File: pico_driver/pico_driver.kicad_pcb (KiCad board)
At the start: 4 copper layers, 65 x 56 mm, 25 parts, among them J1 GPIO, J2 SRV, J3 ESC, J4 ADC, J5 GP_Breakout, J6 VBUS_OUT, J7 3V3_OUT, J8 FUNC, SW1 SW_SPDT, SW2 SW_Push, SW3 SW_Push, U1 Pico

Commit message: update pcb layout
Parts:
- D1: value RKGB -> R K G B
- SW1: value SW_SPDT -> OFF ON
- SW2, SW3: value SW_Push -> PULL_UP
- moved G*** 37.5 mm to (106.6, 57.1)
- moved D1 12.3 mm to (119.3, 90.9), turned to 0 degrees
- moved SW2 0.40 mm to (129.2, 95.7)
- moved J8 0.25 mm to (155.4, 67.8)
- moved SW3 0.22 mm to (143.8, 89.2)
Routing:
- net Net-(D1-BA): track 18.8 -> 6.73 mm
- net Net-(D1-GA): track 14.9 -> 7.08 mm
- net Net-(D1-RA): track 10.1 -> 6.53 mm
- net /SW2: track 21.7 -> 21.1 mm, vias 2 -> 1
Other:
- board text added: "BCDriver 25.05"
- board text removed: "BC Cerebellum V2025.04"

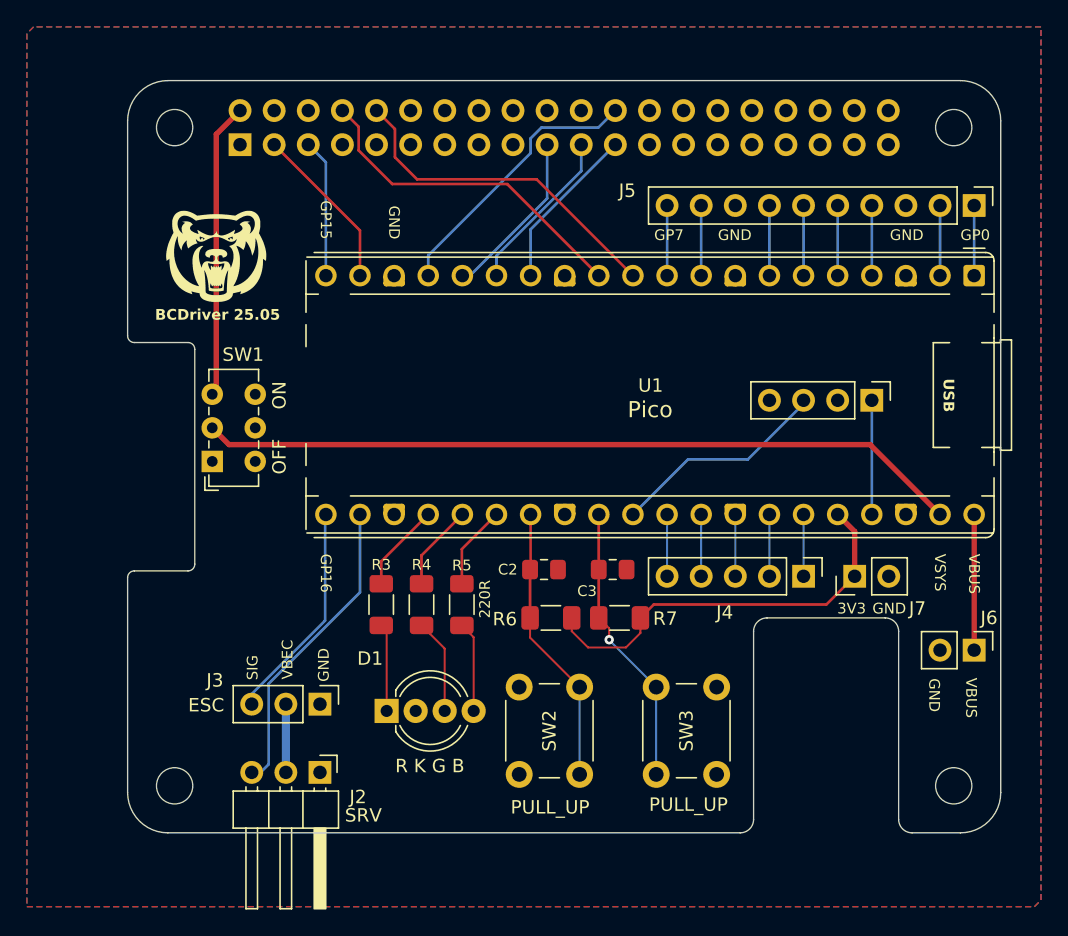
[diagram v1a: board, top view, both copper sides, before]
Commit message: update schemetic and pcb
Pin header for sw1
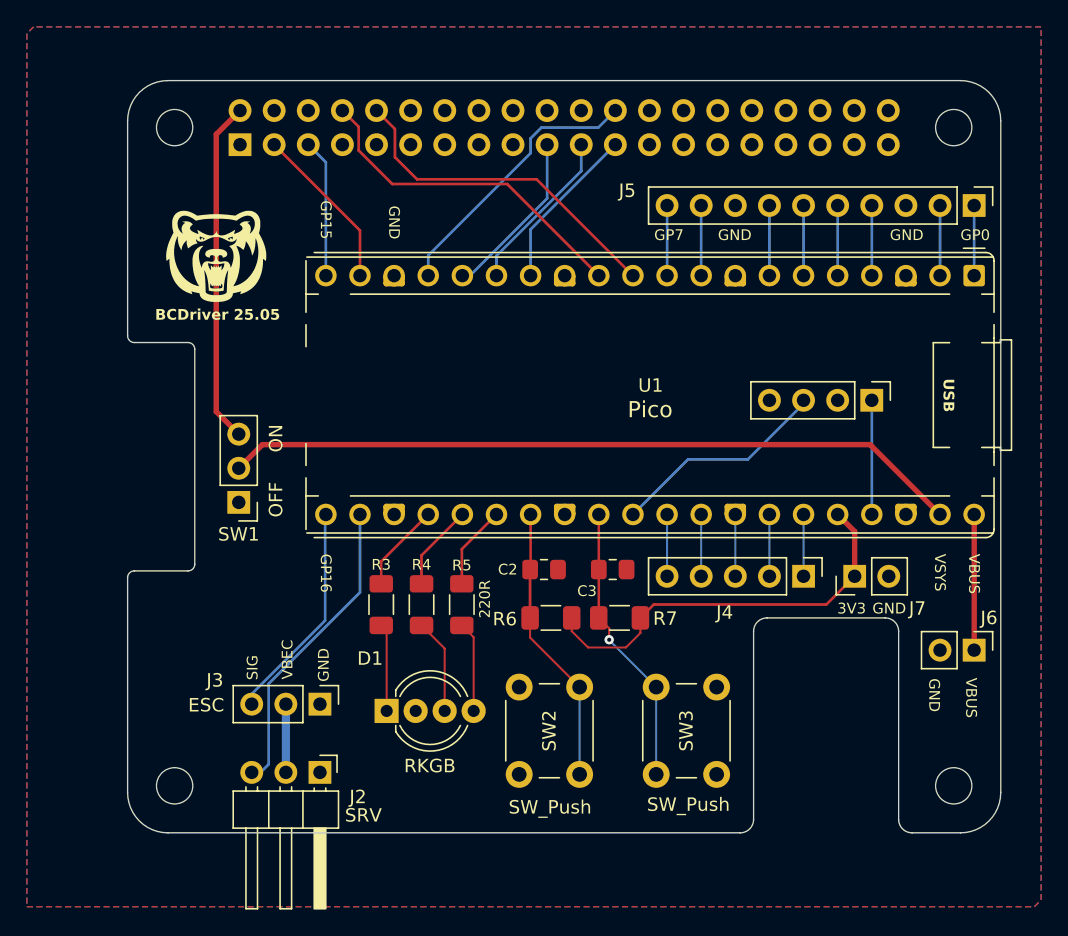
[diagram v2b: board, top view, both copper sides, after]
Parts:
- D1: value R K G B -> RKGB
- SW1: footprint Button_Switch_THT:SW_E-Switch_EG1271_SPDT -> Connector_PinHeader_2.54mm:PinHeader_1x03_P2.54mm_Vertical
- SW2, SW3: value PULL_UP -> SW_Push
- moved SW1 3.63 mm to (108.3, 75.4), turned to 180 degrees
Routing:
- net +5V: track 22.0 -> 25.5 mm
- net VSYS: track 56.9 -> 55.1 mm
